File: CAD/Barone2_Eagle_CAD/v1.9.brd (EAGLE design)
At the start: 101.6 x 101.6 mm, 76 parts, among them J2 XT60-M, M1 PIC32MX340F512H-80I/MR, Q2 BSS138, U1 FT232RQ, X1 CB3LV-3C-8M0000, Y1 ABRACON_ASEK-32_768KHZ-LRTABR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

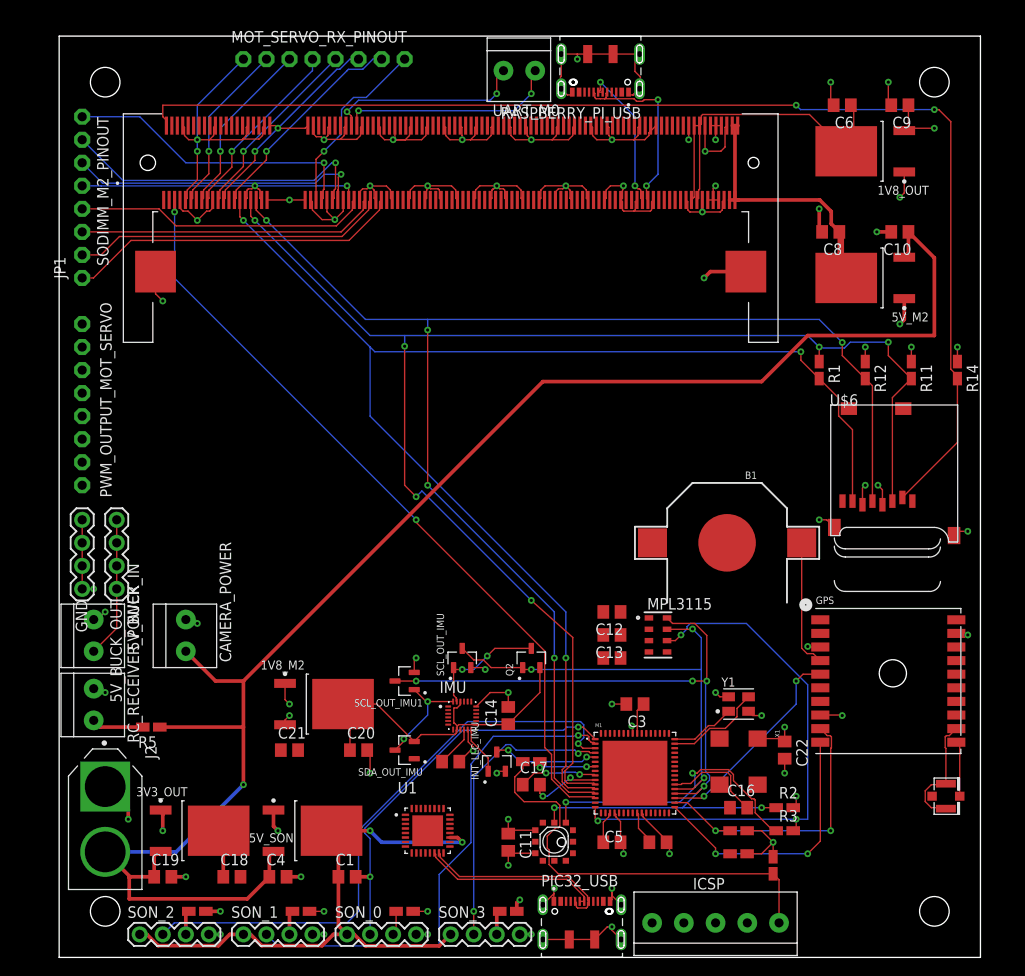
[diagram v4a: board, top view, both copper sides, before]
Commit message: Wiring diagram incomplete, 3.3V and GND via holes bug exists
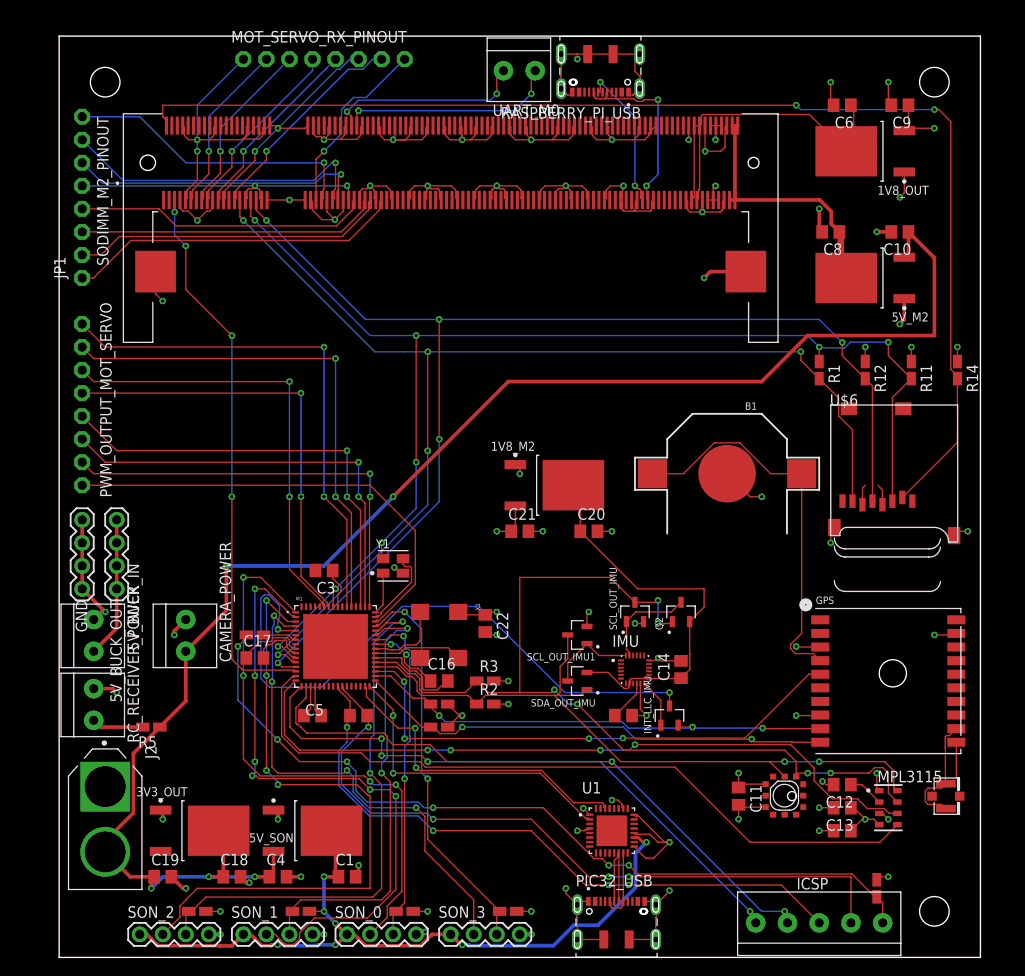
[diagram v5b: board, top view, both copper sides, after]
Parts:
- moved Y1 41.0 mm to (36.8, 43.2)
- moved C3 37.3 mm to (29.2, 42.7)
- moved R3 36.9 mm to (47.0, 30.5)
- moved C15 35.9 mm to (33.0, 26.7)
- moved C16 35.9 mm to (41.9, 30.5)
- moved R7 35.9 mm to (41.9, 27.9)
- moved R8 35.9 mm to (41.9, 25.4)
- moved X1 35.9 mm to (41.9, 35.6)
- moved C22 35.9 mm to (47.0, 36.8)
- moved C5 35.9 mm to (27.9, 26.7)
- moved M1 35.9 mm to (30.5, 34.3)
- moved 1V8_M2 35.0 mm to (54.6, 52.1)
- moved C20 35.0 mm to (58.4, 47.0)
- moved C21 35.0 mm to (50.8, 47.0)
- moved R2 34.9 mm to (47.0, 27.9)
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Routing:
- net INT2_MPL3115: track 0.00 -> 81.0 mm
- net VDD2_M1: track 5.77 -> 78.8 mm, vias 1 -> 4
- net PGED2_M1: track 0.00 -> 68.6 mm, vias 0 -> 2
- net VSS2_M1: track 3.79 -> 71.3 mm, vias 0 -> 4
- net PGEC2_M1: track 0.00 -> 66.8 mm, vias 0 -> 4
- net INT_IMU: track 11.7 -> 70.8 mm
- net ECHO_SON2: track 2.68 -> 60.4 mm, vias 0 -> 2
- net RD6_M1: track 0.00 -> 57.4 mm, vias 0 -> 2
- net RD5_M1: track 0.00 -> 56.6 mm, vias 0 -> 2
- net OC1_M1: track 0.00 -> 50.9 mm
- net RF1_M1: track 0.00 -> 49.8 mm, vias 0 -> 2
- net RF0_M1: track 0.00 -> 49.0 mm, vias 0 -> 2
- net OC4_M1: track 0.00 -> 48.6 mm, vias 0 -> 2
- net OC3_M1: track 0.00 -> 47.8 mm, vias 0 -> 2
- net ECHO_SON1: track 2.68 -> 49.7 mm, vias 0 -> 2
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- added copper zone on layer 15, net 3.3V
- added copper zone on layer 2, net GND

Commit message: Fixed some minor bugs in V1.9 board wiring
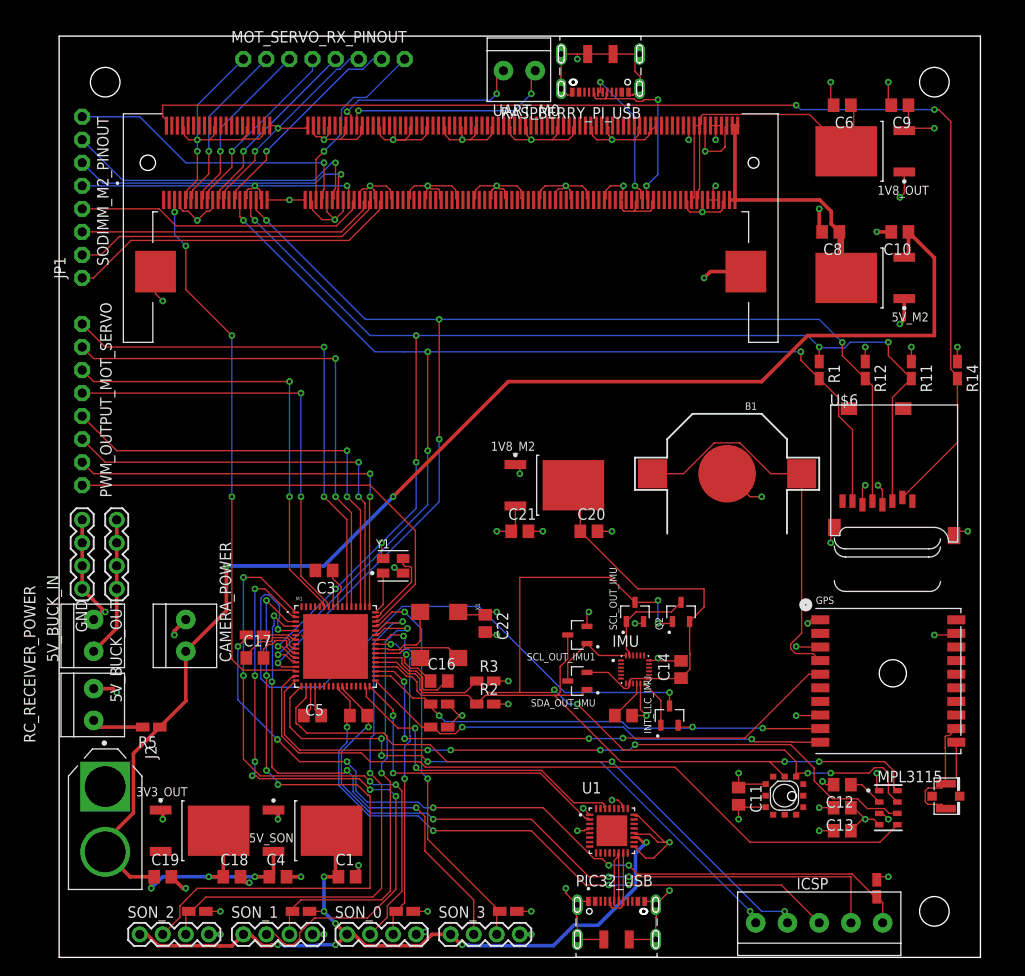
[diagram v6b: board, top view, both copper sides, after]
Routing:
- net EXP: track 0.00 -> 4.30 mm
- net N$1: track 0.00 -> 1.56 mm, vias 0 -> 1
- net GND: track 331.2 -> 331.8 mm
- net VSS: vias 0 -> 1
- net VDD: vias 0 -> 1
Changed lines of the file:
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@@
 <layer number="13" name="Route13" color="21" fill="1" visible="no" active="no"/>
 <layer number="14" name="Route14" color="22" fill="1" visible="no" active="no"/>
-<layer number="15" name="Route15" color="23" fill="1" visible="yes" active="yes"/>
+<layer number="15" name="Route15" color="23" fill="1" visible="no" active="yes"/>
 <layer number="16" name="Bottom" color="1" fill="1" visible="yes" active="yes"/>
 <layer number="17" name="Pads" color="2" fill="1" visible="yes" active="yes"/>
@@
 </element>
 <element name="5V_BUCK_IN" library="adafruit" library_urn="urn:adsk.eagle:library:420" package="1X2-3.5MM" package3d_urn="urn:adsk.eagle:package:6240635/1" value="1X2-3.5MM" x="3.81" y="35.56" smashed="yes" rot="R270">
-<attribute name="NAME" x="8.81" y="33.83" size="1.27" layer="25" rot="R90"/>
+<attribute name="NAME" x="-0.08" y="32.56" size="1.27" layer="25" rot="R90"/>
 </element>
 <element name="RC_RECEIVER_POWER" library="adafruit" library_urn="urn:adsk.eagle:library:420" package="1X2-3.5MM" package3d_urn="urn:adsk.eagle:package:6240635/1" value="1X2-3.5MM" x="3.81" y="27.94" smashed="yes" rot="R270">
-<attribute name="NAME" x="8.81" y="23.67" size="1.27" layer="25" rot="R90"/>
+<attribute name="NAME" x="-2.62" y="23.67" size="1.27" layer="25" rot="R90"/>
 </element>
 <element name="R5" library="adafruit" library_urn="urn:adsk.eagle:library:420" package="R0805W" package3d_urn="urn:adsk.eagle:package:6240567/1" value="47k" x="10.16" y="25.4" smashed="yes" rot="R180">
@@
 <contactref element="M1" pad="65"/>
 <contactref element="U1" pad="33"/>
-<wire x1="30.48" y1="34.29" x2="60.96" y2="13.97" width="0" layer="19" extent="1-1"/>
+<wire x1="30.48" y1="34.29" x2="27.9736" y2="34.29" width="0.1524" layer="1"/>
+<wire x1="27.9736" y1="34.29" x2="26.7036" y2="35.56" width="0.1524" layer="1"/>
+<wire x1="60.96" y1="13.97" x2="30.48" y2="34.29" width="0" layer="19" extent="1-1"/>
 </signal>
 <signal name="GND">
@@
 <wire x1="57.15" y1="99.62" x2="57.15" y2="99.06" width="0.1524" layer="1"/>
 <via x="57.15" y="99.06" extent="1-2" drill="0.35"/>
-<wire x1="55.37" y1="95.795" x2="56.0522" y2="95.1128" width="0.1524" layer="1"/>
-<wire x1="56.0522" y1="95.1128" x2="56.59" y2="95.1128" width="0.1524" layer="1"/>
 <wire x1="64.01" y1="95.795" x2="63.3278" y2="95.1128" width="0.1524" layer="1"/>
 <wire x1="63.3278" y1="95.1128" x2="63.2728875" y2="95.1128" width="0.1524" layer="1"/>
@@
 <wire x1="63.8336" y1="90.6353125" x2="63.3682875" y2="90.17" width="0.1524" layer="1"/>
 <wire x1="63.3682875" y1="90.17" x2="60.96" y2="90.17" width="0.1524" layer="1"/>
-<wire x1="65.83" y1="91.73" x2="65.0336" y2="90.9336" width="0.1524" layer="1"/>
+<wire x1="65.83" y1="91.73" x2="65.23" y2="91.13" width="0.1524" layer="1"/>
+<wire x1="65.155" y1="91.055" x2="65.0336" y2="90.9336" width="0.1524" layer="1"/>
 <wire x1="65.0336" y1="90.9336" x2="65.0336" y2="90.6353125" width="0.1524" layer="1"/>
 <wire x1="65.0336" y1="90.6353125" x2="64.5682875" y2="90.17" width="0.1524" layer="1"/>
@@
 <vertex x="-1.27" y="101.6"/>
 </polygon>
-<wire x1="65.83" y1="91.73" x2="65.23" y2="91.73" width="0" layer="19" extent="1-1"/>
-<wire x1="62.79" y1="95.42" x2="62.79" y2="95.1128" width="0" layer="19" extent="1-1"/>
+<wire x1="55.37" y1="95.795" x2="56.0522" y2="95.1128" width="0.1524" layer="1"/>
+<wire x1="56.0522" y1="95.1128" x2="56.59" y2="95.1128" width="0.1524" layer="1"/>
+<wire x1="65.23" y1="91.73" x2="65.23" y2="91.13" width="0.1524" layer="1"/>
+<wire x1="65.23" y1="91.13" x2="65.155" y2="91.055" width="0.1524" layer="1"/>
+<wire x1="62.79" y1="95.1128" x2="62.79" y2="95.42" width="0" layer="19" extent="1-1"/>
 <wire x1="56.59" y1="95.42" x2="56.59" y2="95.1128" width="0" layer="19" extent="1-1"/>
 <wire x1="39.81" y1="33.02" x2="46.99" y2="35.88" width="0" layer="19" extent="1-1"/>
@@
 <wire x1="18.4432" y1="38.2332" x2="13.97" y2="33.76" width="0.4064" layer="1"/>
 <wire x1="77.47" y1="63.5" x2="49.53" y2="63.5" width="0.4064" layer="1"/>
-<wire x1="10.48" y1="8.89" x2="11.194" y2="11.69" width="0" layer="19" extent="1-1"/>
+<wire x1="5.08" y1="11.64" x2="11.194" y2="11.69" width="0" layer="19" extent="1-1"/>
 </signal>
 <signal name="GND1">
@@
 <wire x1="90.79" y1="49.92" x2="90.79" y2="51.5768" width="0.1524" layer="1"/>
 <wire x1="90.79" y1="51.5768" x2="90.2968" y2="52.07" width="0.1524" layer="1"/>
+<via x="90.2968" y="52.07" extent="1-15" drill="0.35"/>
 </signal>
 <signal name="VSS">
@@
 <wire x1="88.59" y1="49.92" x2="88.59" y2="51.76" width="0.1524" layer="1"/>
 <wire x1="88.59" y1="51.76" x2="88.9" y2="52.07" width="0.1524" layer="1"/>
+<via x="88.9" y="52.07" extent="1-2" drill="0.35"/>
 </signal>
 <signal name="ECHO_SON2">
@@
 <signal name="N$1">
 <contactref element="GPS" pad="P$1"/>
+<wire x1="83.94" y1="37.23" x2="82.95" y2="37.23" width="0.1524" layer="1"/>
+<wire x1="82.95" y1="37.23" x2="82.55" y2="36.83" width="0.1524" layer="1"/>
+<via x="82.55" y="36.83" extent="1-15" drill="0.35"/>
 </signal>
 <signal name="N$6">

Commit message: Fixed GND and 3.3V via issues, currently validating DRC errors
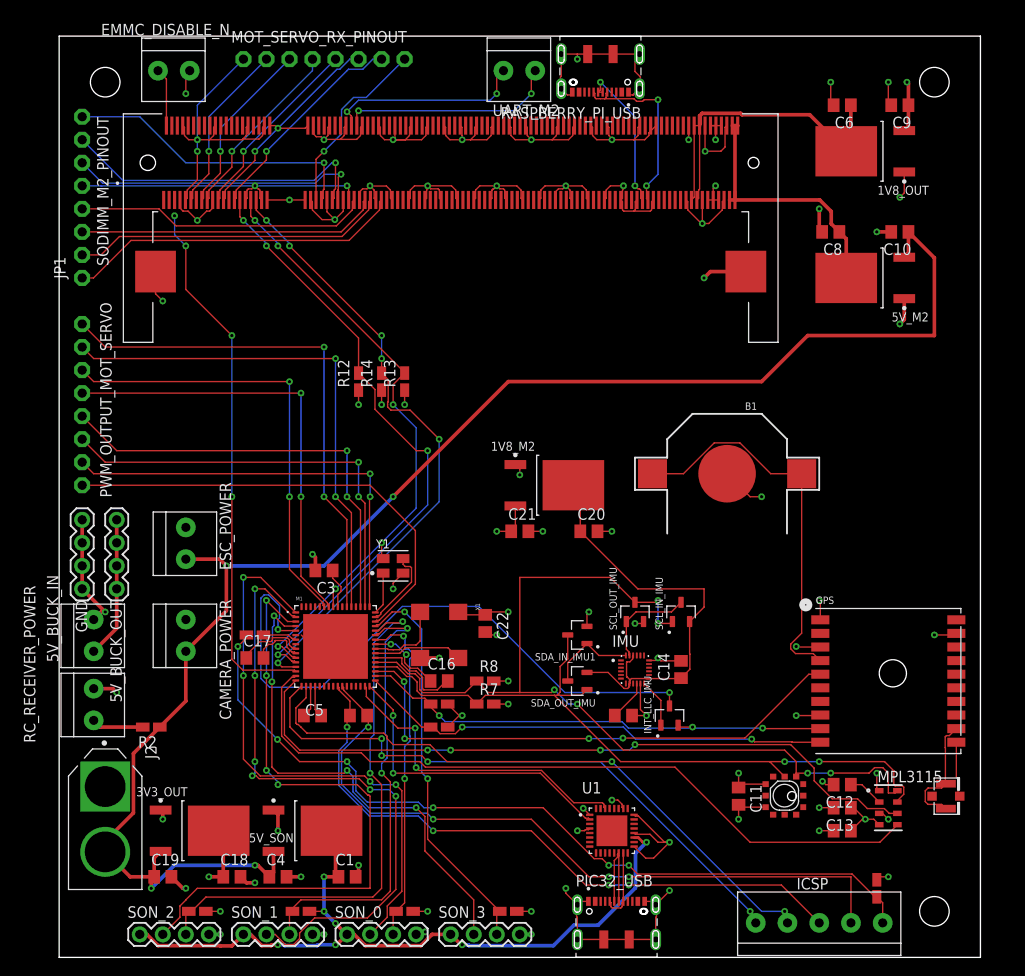
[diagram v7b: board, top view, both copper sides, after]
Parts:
- removed R15: 470, adafruit:R0805W
- removed R16: 10k, adafruit:R0805W
- removed U$6: MICROSD, adafruit:MICROSD
- added EMMC_DISABLE_N, ESC_POWER: 1X2-3.5MM, adafruit:1X2-3.5MM
- added R6: 10k, adafruit:R0805W
- R1: value 47k -> 470
- R11, R5: value 47k -> 10k
- R13: value 10k -> 47k
- R2: value 10k -> 680
- moved R1 68.7 mm to (21.6, 35.6), turned to 180 degrees
- moved R14 63.5 mm to (35.6, 63.5), turned to 90 degrees
- moved R13 59.5 mm to (38.1, 63.5), turned to 90 degrees
- moved R11 57.3 mm to (90.2, 7.62)
- moved R12 55.9 mm to (33.0, 63.5), turned to 90 degrees
- moved R2 36.9 mm to (10.2, 25.4), turned to 180 degrees
- moved R10 33.5 mm to (41.9, 25.4), turned to 0 degrees
- moved R9 27.5 mm to (41.9, 27.9), turned to 0 degrees
- moved R3 26.9 mm to (38.1, 5.08), turned to 180 degrees
- moved R5 20.9 mm to (15.2, 5.08)
- moved R4 11.4 mm to (26.7, 5.08)
- moved R8 7.18 mm to (47.0, 30.5)
- moved R7 5.08 mm to (47.0, 27.9)
- renumbered Q2 to SCL_IN_IMU, SCL_OUT_IMU1 to SDA_IN_IMU1, UART_M0 to UART_M2
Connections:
- removed net 3.3V: 3V3_OUT.4, C18.1
- removed net CS_MICRO_SD: R14.2, SODIMM_M2_PINOUT.2, U$6.2
- removed net GND1: U$6.MT1, U$6.MT2
- removed net VDD: U$6.4
- removed net VSS: U$6.6
- new net N$4: EMMC_DISABLE_N.1, SODIMM_M2_PINOUT.2
- net 9.6V-12.6V: now also ESC_POWER.1, R2.1; no longer R5.1
- net CS_M1: no longer SODIMM_M2_PINOUT.5
- net ECHO_SON0: now also R3.2; no longer R4.2
- net ECHO_SON1: now also R4.2; no longer R9.2
- net ECHO_SON2: now also R5.2; no longer R10.2
- net ECHO_SON3: now also R6.2; no longer R13.2
- net GND: now also EMMC_DISABLE_N.2, ESC_POWER.2, R3.1, R5.1, R6.1; no longer R10.1, R13.1, R9.1
- net MCLR_M1: now also R1.2, R11.2; no longer R15.2, R16.2
- net MISO_M2: now also R12.2; no longer R1.2, U$6.7
- net MOSI_M2: now also R13.2; no longer R11.2, U$6.3
- net N$13: now also R1.1; no longer R15.1
- net N$14: now also R2.2; no longer R5.2
- net SCK_M2: now also R14.2; no longer R12.2, U$6.5
- net SCL_M1: now also MPL3115.8, R8.1; no longer MPL3115.7, R3.1
- net SDA_M1: now also MPL3115.7, R7.1; no longer MPL3115.8, R2.1
- net U1RX_M1: now also R9.1; no longer R7.1
- net U1TX_M1: now also R10.1; no longer R8.1
- net VIN: now also 3V3_OUT.4, C18.1, R10.2, R13.1, R9.2; no longer R1.1, R16.1, R2.2, R3.2
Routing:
- net GND: track 331.8 -> 938.2 mm, vias 65 -> 67
- net VIN: track 66.8 -> 365.3 mm
- net CS_MICRO_SD: track 134.3 -> 0.00 mm, vias 2 -> 0
- net MOSI_M2: track 140.9 -> 66.6 mm, vias 5 -> 4
- net SCK_M2: track 138.1 -> 70.4 mm, vias 5 -> 6
- net MISO_M2: track 131.3 -> 68.6 mm, vias 5 -> 4
- net 1.8V: track 84.6 -> 96.9 mm
- net 9.6V-12.6V: track 165.8 -> 174.7 mm
- net 3.3V: track 6.88 -> 0.00 mm, vias 1 -> 0
- net N$4: track 0.00 -> 6.45 mm
- net GND1: track 3.58 -> 0.00 mm, vias 2 -> 0
- net VDD: track 2.35 -> 0.00 mm, vias 1 -> 0
- net SDA_M1: track 79.0 -> 81.3 mm
- net VSS: track 2.28 -> 0.00 mm, vias 1 -> 0
- net 5V: track 112.3 -> 110.2 mm
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- removed copper zone on layer 15, net 3.3V
- removed copper zone on layer 2, net GND

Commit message: Added GND to A0 pin of ICM-20948 IMU sensor, removed one 1.8V and 5.0V voltage regulators.
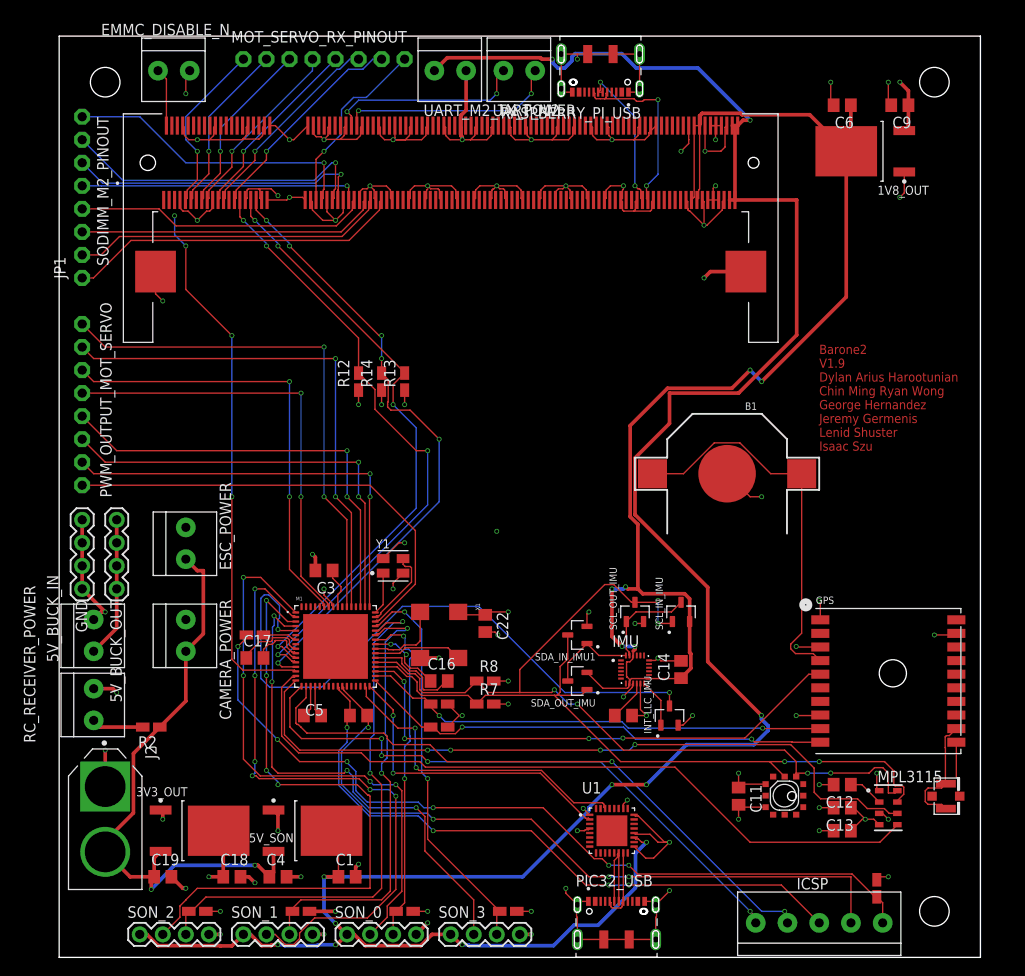
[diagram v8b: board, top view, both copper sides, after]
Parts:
- removed 1V8_M2, 5V_M2: STMICROELECTRONICS_LD1117DT33CTRSTMICROELECTRONICS_LD1117DT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, STMicroelectronics - LD1117DT33CTR:STMICROELECTRONICS_LD1117DT33CTR_2
- removed C10, C21: 0.1uF, rcl:C0805
- removed C20, C8: 10uF, rcl:C0805
- added UART_M2_TX_POWER: 1X2-3.5MM, adafruit:1X2-3.5MM
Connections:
- removed net N$1: GPS.P$1
- net 1.8V: no longer 1V8_M2.4, C20.1
- net 5V: now also UART_M2_TX_POWER.1; no longer 5V_M2.4, C8.1
- net 9.6V-12.6V: no longer 5V_M2.3, C10.1
- net GND: now also IMU.9, UART_M2_TX_POWER.2; no longer 1V8_M2.1, 5V_M2.1, C10.2, C20.2, C21.2, C8.2
- net VIN: now also GPS.P$1; no longer 1V8_M2.3, C21.1
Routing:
- net 5V: track 110.2 -> 273.3 mm, vias 6 -> 11
- net 9.6V-12.6V: track 174.7 -> 66.9 mm, vias 4 -> 2
- net 1.8V: track 96.9 -> 156.8 mm, vias 0 -> 6
- net VIN: track 365.3 -> 405.4 mm, vias 24 -> 25
- net GND: track 938.2 -> 919.8 mm, vias 67 -> 62
- net SCL_M1: track 102.0 -> 95.4 mm
- net EXP: track 4.30 -> 0.00 mm
- net N$1: track 2.19 -> 0.00 mm, vias 1 -> 0
- net GPIO2_M2: track 18.2 -> 19.2 mm
- net INT1_MPL3115: track 79.0 -> 79.8 mm
- added copper zone on layer 2, net GND
- added copper zone on layer 15, net VIN
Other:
- board text added: "Barone2 V1.9 Dylan Arius Harootunian Chin Ming Ryan Wong George Hernandez Jeremy Germenis Lenid Shuster Isaac Szu"
